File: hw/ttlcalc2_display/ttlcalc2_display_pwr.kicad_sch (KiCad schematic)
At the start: 9 parts, among them U11 74LS04, U12 74LS04, U14 74LS04, U17 74LS04, U18 74LS04, U19 74LS139, U3 74LS08, U4 74LS139, U8 74LS04

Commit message: Continue work on display driver board schematic
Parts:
- added C1, C10, C11, C12, C13, C14, C15, C16, C17, C18, C19, C2, C20, C21, C22, C23, C3, C4, C5, C6, C7, C8, C9: C, Capacitor_THT:C_Disc_D5.0mm_W2.5mm_P5.00mm, symbol Device:C
- added U23: 74LS02, Package_DIP:DIP-14_W7.62mm, symbol 74xx:74LS02
- renumbered U8 to U10, U12 to U13, U4 to U3, U3 to U5
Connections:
- net GND: now also C1.2, C10.2, C11.2, C12.2, C13.2, C14.2, C15.2, C16.2, C17.2, C18.2, C19.2, C2.2, C20.2, C21.2, C22.2, C23.2, C3.2, C4.2, C5.2, C6.2, C7.2, C8.2, C9.2, U23.7 (GND)
- net VCC: now also C1.1, C10.1, C11.1, C12.1, C13.1, C14.1, C15.1, C16.1, C17.1, C18.1, C19.1, C2.1, C20.1, C21.1, C22.1, C23.1, C3.1, C4.1, C5.1, C6.1, C7.1, C8.1, C9.1, U23.14 (VCC)

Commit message: Simplify display driver board, add busy light
Removed digit storage and multiplexing logic from display driver, will handle in software instead
Add driver for busy indicator
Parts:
- removed U19: 74LS139, Package_DIP:DIP-16_W7.62mm, symbol 74xx:74LS139
- removed U23: 74LS02, Package_DIP:DIP-14_W7.62mm, symbol 74xx:74LS02
- added C24: 1000u, Capacitor_THT:CP_Radial_D10.0mm_P5.00mm, symbol Device:C_Polarized_US
- added C25: 100u, Capacitor_THT:CP_Radial_D18.0mm_P7.50mm, symbol Device:C_Polarized_US
- added J3: 5V_PWR, TerminalBlock_Phoenix:TerminalBlock_Phoenix_MKDS-1,5-2-5.08_1x02_P5.08mm_Horizontal, symbol Connector_Generic:Conn_01x02
- added J4: HV_PWR, TerminalBlock_Phoenix:TerminalBlock_Phoenix_MKDS-1,5-2-5.08_1x02_P5.08mm_Horizontal, symbol Connector_Generic:Conn_01x02
- renumbered C21 to C10, C6 to C11, C22 to C12, C7 to C13, C23 to C14, C8 to C15, C9 to C16, C10 to C17, C11 to C18, C12 to C19, C17 to C2, C13 to C20, C14 to C21, C15 to C22, C16 to C23, C2 to C3, C18 to C4, C3 to C5, C19 to C6, C4 to C7, C20 to C8, C5 to C9, U3 to U1, U5 to U6
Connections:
- net GND: now also C24.2, C25.2, J3.2 (Pin_2), J4.2 (Pin_2)
- net VCC: now also C24.1, J3.1 (Pin_1)
- new net HT: C25.1, J4.1 (Pin_1)

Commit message: Minor simplifications and ERC fix
Fix missing NE_BUSY from bus definition
Switch 74LS139 to 74LS138
Remove extra bypass caps
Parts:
- removed C10, C2, C4, C6, C8: C, Capacitor_THT:C_Disc_D5.0mm_W2.5mm_P5.00mm, symbol Device:C
- removed U1: 74LS139, Package_DIP:DIP-16_W7.62mm, symbol 74xx:74LS139
- renumbered C17 to C10, C18 to C11, C19 to C12, C20 to C13, C21 to C14, C22 to C15, C23 to C16, C12 to C17, C14 to C18, C24 to C19, C3 to C2, C25 to C20, C5 to C3, C7 to C4, C9 to C5, C11 to C6, C13 to C7, C15 to C8, C16 to C9
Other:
- moved on the sheet: C17, C18

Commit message: Display driver board routing and silkscreen tweaks
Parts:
- added C19: C, Capacitor_THT:C_Axial_L3.8mm_D2.6mm_P7.50mm_Horizontal, symbol Device:C
- added U19: 74LS04, Package_DIP:DIP-14_W7.62mm, symbol 74xx:74LS04
- C1, C10, C11, C12, C13, C14, C15, C16, C17, C18, C2, C3, C4, C5, C6, C7, C8, C9: footprint Capacitor_THT:C_Disc_D5.0mm_W2.5mm_P5.00mm -> Capacitor_THT:C_Axial_L3.8mm_D2.6mm_P7.50mm_Horizontal
- C100: renamed from C19; value 1000u -> 100u; footprint Capacitor_THT:CP_Radial_D10.0mm_P5.00mm -> Capacitor_THT:CP_Radial_D6.3mm_P2.50mm
- renumbered C20 to C101
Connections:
- net GND: now also J3.1 (Pin_1), J4.1 (Pin_1), C19.2, U19.7 (GND); no longer J3.2 (Pin_2), J4.2 (Pin_2)
- net HT: now also J4.2 (Pin_2); no longer J4.1 (Pin_1)
- net VCC: now also J3.2 (Pin_2), C19.1, U19.14 (VCC); no longer J3.1 (Pin_1)

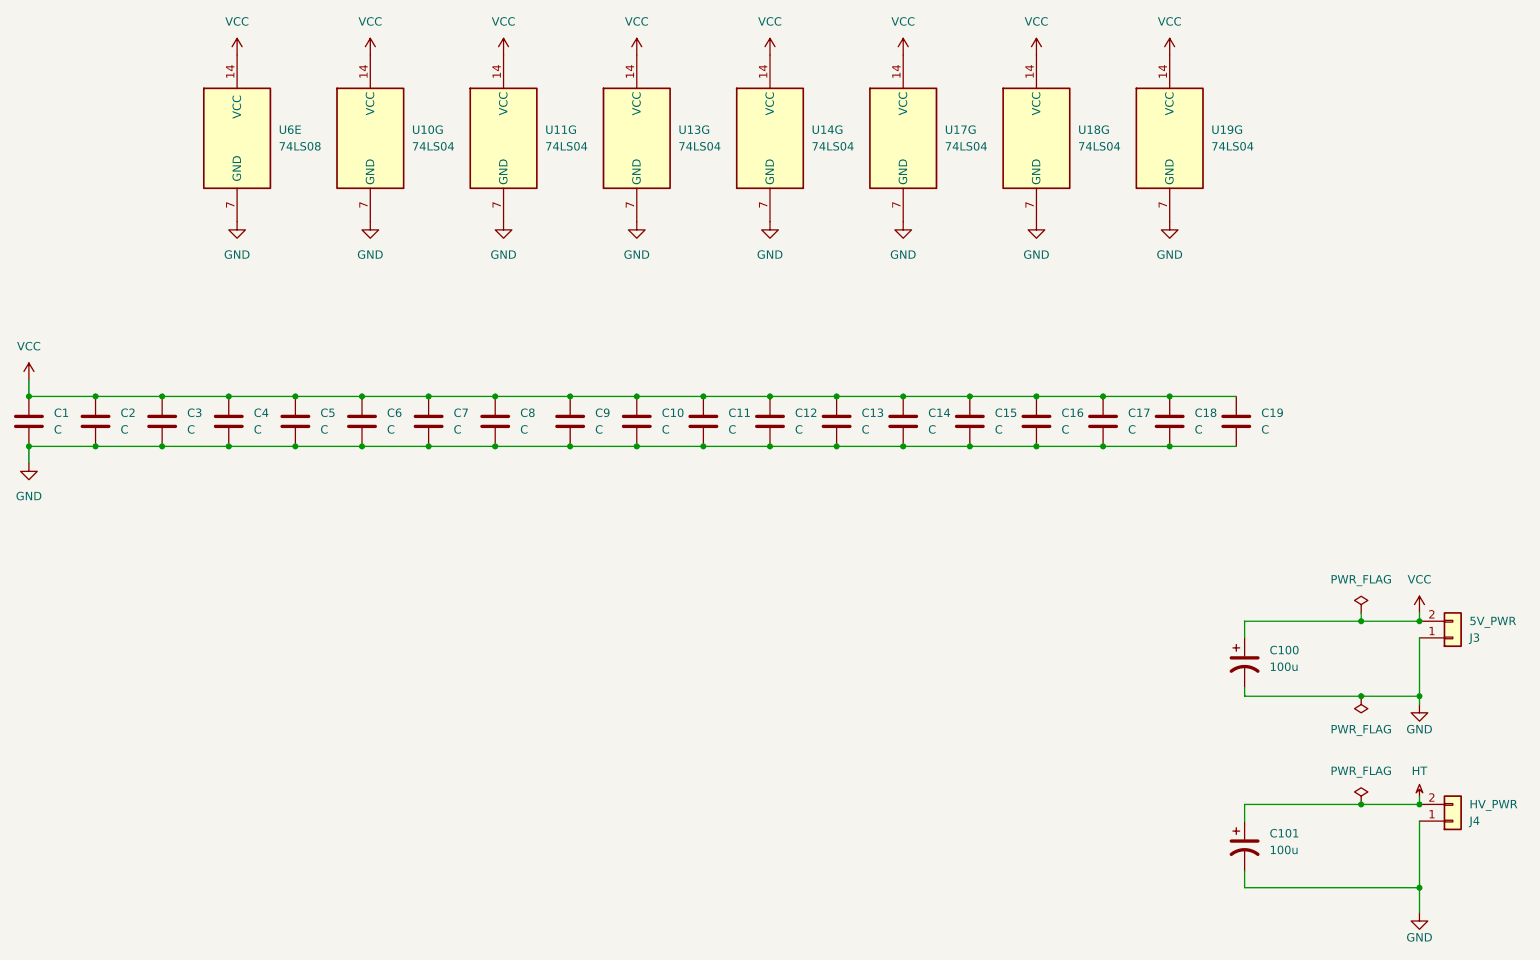
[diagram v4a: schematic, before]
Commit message: Display driver geographical reannotate
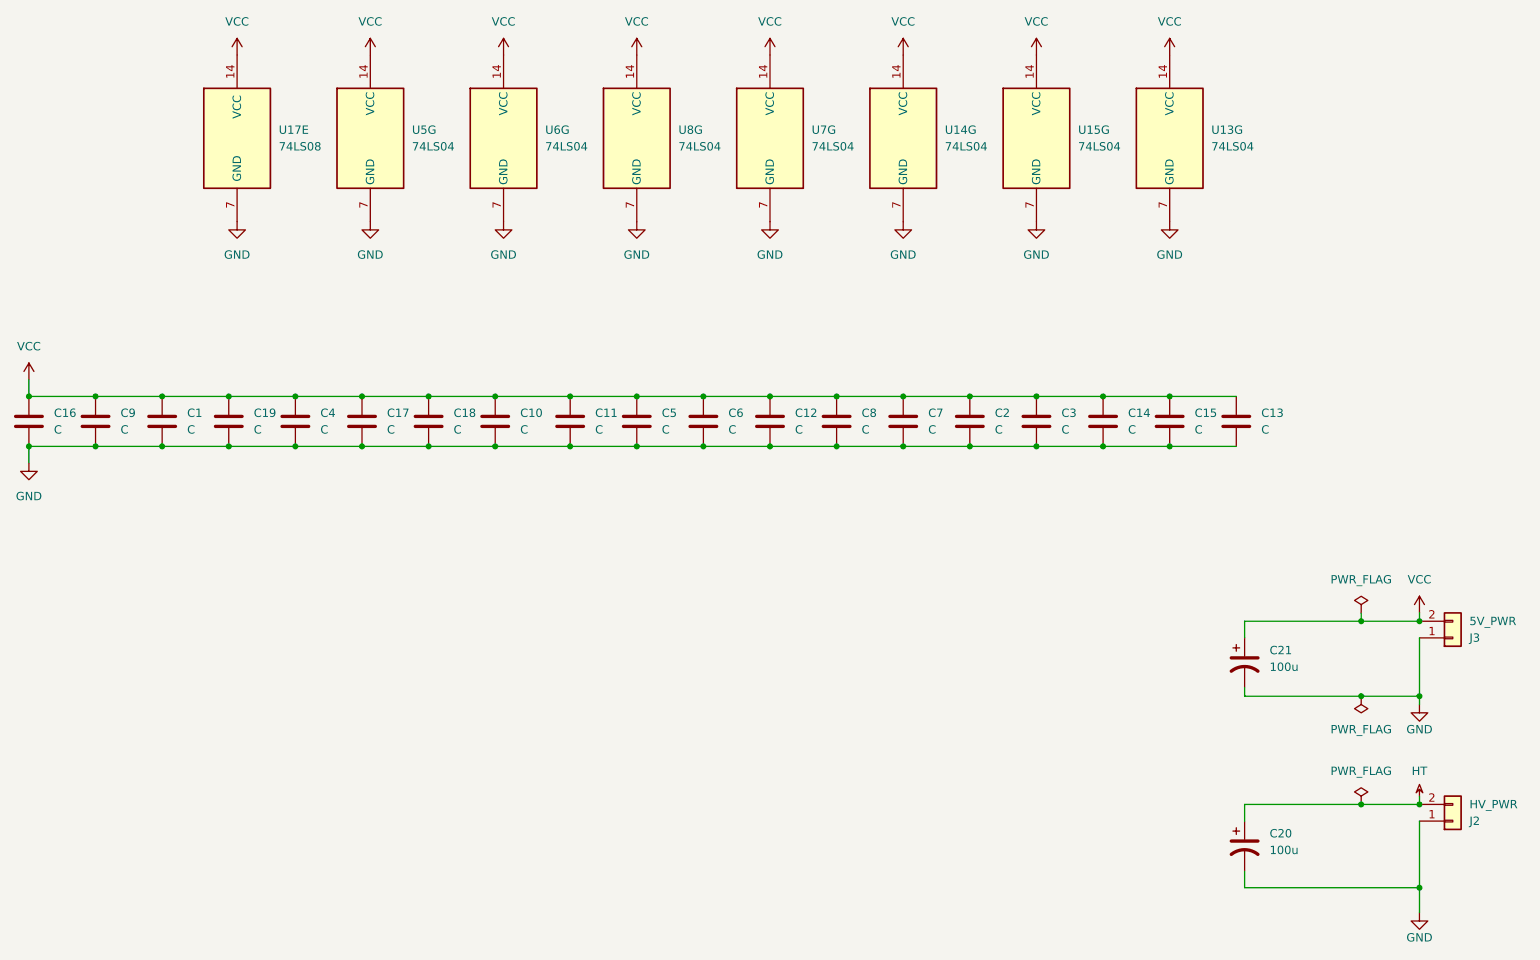
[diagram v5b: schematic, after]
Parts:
- renumbered C3 to C1, C8 to C10, C9 to C11, C19 to C13, C17 to C14, C18 to C15, C1 to C16, C6 to C17, C7 to C18, C4 to C19, C15 to C2, C101 to C20, C100 to C21, C16 to C3, C5 to C4, C10 to C5, C11 to C6, C14 to C7, C13 to C8, C2 to C9, J4 to J2, U19 to U13, U17 to U14, U18 to U15, U6 to U17, U10 to U5, U11 to U6, U14 to U7, U13 to U8
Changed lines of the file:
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@@
 		(dnp no)
 		(fields_autoplaced yes)
-		(property "Reference" "C15"
+		(property "Reference" "C2"
 			(at 172.72 78.7399 0)
 			(effects
@@
 			(project "ttlcalc2_display"
 				(path "/4da693c8-a60c-4d11-a405-739e88984bfc/bbab562b-1662-4bba-86e9-b87ed8790691"
-					(reference "C15")
+					(reference "C2")
 					(unit 1)
 				)
@@
 		(dnp no)
 		(fields_autoplaced yes)
-		(property "Reference" "C7"
+		(property "Reference" "C18"
 			(at 90.17 78.7399 0)
 			(effects
@@
 			(project "ttlcalc2_display"
 				(path "/4da693c8-a60c-4d11-a405-739e88984bfc/bbab562b-1662-4bba-86e9-b87ed8790691"
-					(reference "C7")
+					(reference "C18")
 					(unit 1)
 				)
@@
 		(dnp no)
 		(fields_autoplaced yes)
-		(property "Reference" "U13"
+		(property "Reference" "U8"
 			(at 124.46 35.5599 0)
 			(effects
@@
 			(project "ttlcalc2_display"
 				(path "/4da693c8-a60c-4d11-a405-739e88984bfc/bbab562b-1662-4bba-86e9-b87ed8790691"
-					(reference "U13")
+					(reference "U8")
 					(unit 7)
 				)
@@
 		(dnp no)
 		(fields_autoplaced yes)
-		(property "Reference" "C8"
+		(property "Reference" "C10"
 			(at 100.33 78.7399 0)
 			(effects
@@
 			(project "ttlcalc2_display"
 				(path "/4da693c8-a60c-4d11-a405-739e88984bfc/bbab562b-1662-4bba-86e9-b87ed8790691"
-					(reference "C8")
+					(reference "C10")
 					(unit 1)
 				)
@@
 		(dnp no)
 		(fields_autoplaced yes)
-		(property "Reference" "U6"
+		(property "Reference" "U17"
 			(at 63.5 35.5599 0)
 			(effects
@@
 			(project "ttlcalc2_display"
 				(path "/4da693c8-a60c-4d11-a405-739e88984bfc/bbab562b-1662-4bba-86e9-b87ed8790691"
-					(reference "U6")
+					(reference "U17")
 					(unit 5)
 				)
@@
 		(dnp no)
 		(fields_autoplaced yes)
-		(property "Reference" "C6"
+		(property "Reference" "C17"
 			(at 80.01 78.7399 0)
 			(effects
@@
 			(project "ttlcalc2_display"
 				(path "/4da693c8-a60c-4d11-a405-739e88984bfc/bbab562b-1662-4bba-86e9-b87ed8790691"
-					(reference "C6")
+					(reference "C17")
 					(unit 1)
 				)
@@
 		(dnp no)
 		(fields_autoplaced yes)
-		(property "Reference" "C2"
+		(property "Reference" "C9"
 			(at 39.37 78.7399 0)
 			(effects
@@
 			(project "ttlcalc2_display"
 				(path "/4da693c8-a60c-4d11-a405-739e88984bfc/bbab562b-1662-4bba-86e9-b87ed8790691"
-					(reference "C2")
+					(reference "C9")
 					(unit 1)
 				)
@@
 		(dnp no)
 		(fields_autoplaced yes)
-		(property "Reference" "C5"
+		(property "Reference" "C4"
 			(at 69.85 78.7399 0)
 			(effects
@@
 			(project "ttlcalc2_display"
 				(path "/4da693c8-a60c-4d11-a405-739e88984bfc/bbab562b-1662-4bba-86e9-b87ed8790691"
-					(reference "C5")
+					(reference "C4")
 					(unit 1)
 				)
@@
 		(dnp no)
 		(fields_autoplaced yes)
-		(property "Reference" "U17"
+		(property "Reference" "U14"
 			(at 165.1 35.5599 0)
 			(effects
@@
 			(project "ttlcalc2_display"
 				(path "/4da693c8-a60c-4d11-a405-739e88984bfc/bbab562b-1662-4bba-86e9-b87ed8790691"
-					(reference "U17")
+					(reference "U14")
 					(unit 7)
 				)
@@
 		(dnp no)
 		(fields_autoplaced yes)
-		(property "Reference" "U18"
+		(property "Reference" "U15"
 			(at 185.42 35.5599 0)
 			(effects
@@
 			(project "ttlcalc2_display"
 				(path "/4da693c8-a60c-4d11-a405-739e88984bfc/bbab562b-1662-4bba-86e9-b87ed8790691"
-					(reference "U18")
+					(reference "U15")
 					(unit 7)
 				)
@@
 		(dnp no)
 		(fields_autoplaced yes)
-		(property "Reference" "U19"
+		(property "Reference" "U13"
 			(at 205.74 35.5599 0)
 			(effects
@@
 			(project "ttlcalc2_display"
 				(path "/4da693c8-a60c-4d11-a405-739e88984bfc/bbab562b-1662-4bba-86e9-b87ed8790691"
-					(reference "U19")
+					(reference "U13")
 					(unit 7)
 				)
@@
 		(dnp no)
 		(fields_autoplaced yes)
-		(property "Reference" "C11"
+		(property "Reference" "C6"
 			(at 132.08 78.7399 0)
 			(effects
@@
 			(project "ttlcalc2_display"
 				(path "/4da693c8-a60c-4d11-a405-739e88984bfc/bbab562b-1662-4bba-86e9-b87ed8790691"
-					(reference "C11")
+					(reference "C6")
 					(unit 1)
 				)
@@
 		(dnp no)
 		(fields_autoplaced yes)
-		(property "Reference" "C16"
+		(property "Reference" "C3"
 			(at 182.88 78.7399 0)
 			(effects
@@
 			(project "ttlcalc2_display"
 				(path "/4da693c8-a60c-4d11-a405-739e88984bfc/bbab562b-1662-4bba-86e9-b87ed8790691"
-					(reference "C16")
+					(reference "C3")
 					(unit 1)
 				)
@@
 		(dnp no)
 		(fields_autoplaced yes)
-		(property "Reference" "C10"
+		(property "Reference" "C5"
 			(at 121.92 78.7399 0)
 			(effects
@@
 			(project "ttlcalc2_display"
 				(path "/4da693c8-a60c-4d11-a405-739e88984bfc/bbab562b-1662-4bba-86e9-b87ed8790691"
-					(reference "C10")
+					(reference "C5")
 					(unit 1)
 				)
@@
 		(dnp no)
 		(fields_autoplaced yes)
-		(property "Reference" "C19"
+		(property "Reference" "C13"
 			(at 213.36 78.7399 0)
 			(effects
@@
 			(project "ttlcalc2_display"
 				(path "/4da693c8-a60c-4d11-a405-739e88984bfc/bbab562b-1662-4bba-86e9-b87ed8790691"
-					(reference "C19")
+					(reference "C13")
 					(unit 1)
 				)
@@
 		(dnp no)
 		(fields_autoplaced yes)
-		(property "Reference" "C14"
+		(property "Reference" "C7"
 			(at 162.56 78.7399 0)
 			(effects
@@
 			(project "ttlcalc2_display"
 				(path "/4da693c8-a60c-4d11-a405-739e88984bfc/bbab562b-1662-4bba-86e9-b87ed8790691"
-					(reference "C14")
+					(reference "C7")
 					(unit 1)
 				)
@@
 		(dnp no)
 		(fields_autoplaced yes)
-		(property "Reference" "C17"
+		(property "Reference" "C14"
 			(at 193.04 78.7399 0)
 			(effects
@@
 			(project "ttlcalc2_display"
 				(path "/4da693c8-a60c-4d11-a405-739e88984bfc/bbab562b-1662-4bba-86e9-b87ed8790691"
-					(reference "C17")
+					(reference "C14")
 					(unit 1)
 				)
@@
 		(dnp no)
 		(fields_autoplaced yes)
-		(property "Reference" "U14"
+		(property "Reference" "U7"
 			(at 144.78 35.5599 0)
 			(effects
@@
 			(project "ttlcalc2_display"
 				(path "/4da693c8-a60c-4d11-a405-739e88984bfc/bbab562b-1662-4bba-86e9-b87ed8790691"
-					(reference "U14")
+					(reference "U7")
 					(unit 7)
 				)
@@
 		(dnp no)
 		(fields_autoplaced yes)
-		(property "Reference" "C1"
+		(property "Reference" "C16"
 			(at 29.21 78.7399 0)
 			(effects
@@
 			(project ""
 				(path "/4da693c8-a60c-4d11-a405-739e88984bfc/bbab562b-1662-4bba-86e9-b87ed8790691"
-					(reference "C1")
+					(reference "C16")
 					(unit 1)
 				)
@@
 		(on_board yes)
 		(dnp no)
-		(property "Reference" "J4"
+		(property "Reference" "J2"
 			(at 245.11 140.9701 0)
 			(effects
@@
 			(project "ttlcalc2_display"
 				(path "/4da693c8-a60c-4d11-a405-739e88984bfc/bbab562b-1662-4bba-86e9-b87ed8790691"
-					(reference "J4")
+					(reference "J2")
 					(unit 1)
 				)
@@
 		(dnp no)
 		(fields_autoplaced yes)
-		(property "Reference" "C101"
+		(property "Reference" "C20"
 			(at 214.63 142.8749 0)
 			(effects
@@
 			(project "ttlcalc2_display"
 				(path "/4da693c8-a60c-4d11-a405-739e88984bfc/bbab562b-1662-4bba-86e9-b87ed8790691"
-					(reference "C101")
+					(reference "C20")
 					(unit 1)
 				)
@@
 		(dnp no)
 		(fields_autoplaced yes)
-		(property "Reference" "C100"
+		(property "Reference" "C21"
 			(at 214.63 114.9349 0)
 			(effects
@@
 			(project "ttlcalc2_display"
 				(path "/4da693c8-a60c-4d11-a405-739e88984bfc/bbab562b-1662-4bba-86e9-b87ed8790691"
-					(reference "C100")
+					(reference "C21")
 					(unit 1)
 				)
@@
 		(dnp no)
 		(fields_autoplaced yes)
-		(property "Reference" "C4"
+		(property "Reference" "C19"
 			(at 59.69 78.7399 0)
 			(effects
@@
 			(project "ttlcalc2_display"
 				(path "/4da693c8-a60c-4d11-a405-739e88984bfc/bbab562b-1662-4bba-86e9-b87ed8790691"
-					(reference "C4")
+					(reference "C19")
 					(unit 1)
 				)
@@
 		(dnp no)
 		(fields_autoplaced yes)
-		(property "Reference" "C13"
+		(property "Reference" "C8"
 			(at 152.4 78.7399 0)
 			(effects
@@
 			(project "ttlcalc2_display"
 				(path "/4da693c8-a60c-4d11-a405-739e88984bfc/bbab562b-1662-4bba-86e9-b87ed8790691"
-					(reference "C13")
+					(reference "C8")
 					(unit 1)
 				)
@@
 		(dnp no)
 		(fields_autoplaced yes)
-		(property "Reference" "U11"
+		(property "Reference" "U6"
 			(at 104.14 35.5599 0)
 			(effects
@@
 			(project "ttlcalc2_display"
 				(path "/4da693c8-a60c-4d11-a405-739e88984bfc/bbab562b-1662-4bba-86e9-b87ed8790691"
-					(reference "U11")
+					(reference "U6")
 					(unit 7)
 				)
@@
 		(dnp no)
 		(fields_autoplaced yes)
-		(property "Reference" "U10"
+		(property "Reference" "U5"
 			(at 83.82 35.5599 0)
 			(effects
@@
 			(project "ttlcalc2_display"
 				(path "/4da693c8-a60c-4d11-a405-739e88984bfc/bbab562b-1662-4bba-86e9-b87ed8790691"
-					(reference "U10")
+					(reference "U5")
 					(unit 7)
 				)
@@
 		(dnp no)
 		(fields_autoplaced yes)
-		(property "Reference" "C18"
+		(property "Reference" "C15"
 			(at 203.2 78.7399 0)
 			(effects
@@
 			(project "ttlcalc2_display"
 				(path "/4da693c8-a60c-4d11-a405-739e88984bfc/bbab562b-1662-4bba-86e9-b87ed8790691"
-					(reference "C18")
+					(reference "C15")
 					(unit 1)
 				)
@@
 		(dnp no)
 		(fields_autoplaced yes)
-		(property "Reference" "C3"
+		(property "Reference" "C1"
 			(at 49.53 78.7399 0)
 			(effects
@@
 			(project "ttlcalc2_display"
 				(path "/4da693c8-a60c-4d11-a405-739e88984bfc/bbab562b-1662-4bba-86e9-b87ed8790691"
-					(reference "C3")
+					(reference "C1")
 					(unit 1)
 				)
@@
 		(dnp no)
 		(fields_autoplaced yes)
-		(property "Reference" "C9"
+		(property "Reference" "C11"
 			(at 111.76 78.7399 0)
 			(effects
@@
 			(project "ttlcalc2_display"
 				(path "/4da693c8-a60c-4d11-a405-739e88984bfc/bbab562b-1662-4bba-86e9-b87ed8790691"
-					(reference "C9")
+					(reference "C11")
 					(unit 1)
 				)

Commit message: Convert to KiCad 9.0
Convert to KiCad 9.0 format
Tweak silkscreen to fix DRC errors introduced by updated footprints
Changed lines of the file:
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@@
 (kicad_sch
-	(version 20231120)
+	(version 20250114)
 	(generator "eeschema")
-	(generator_version "8.0")
+	(generator_version "9.0")
 	(paper "USLetter")
 	(title_block
